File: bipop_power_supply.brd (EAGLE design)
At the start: 82.5 x 70.8 mm, 33 parts, among them IC1 LM1117MP-3.3, IC2 LM1117MP-5.0, X2 MSTBA6

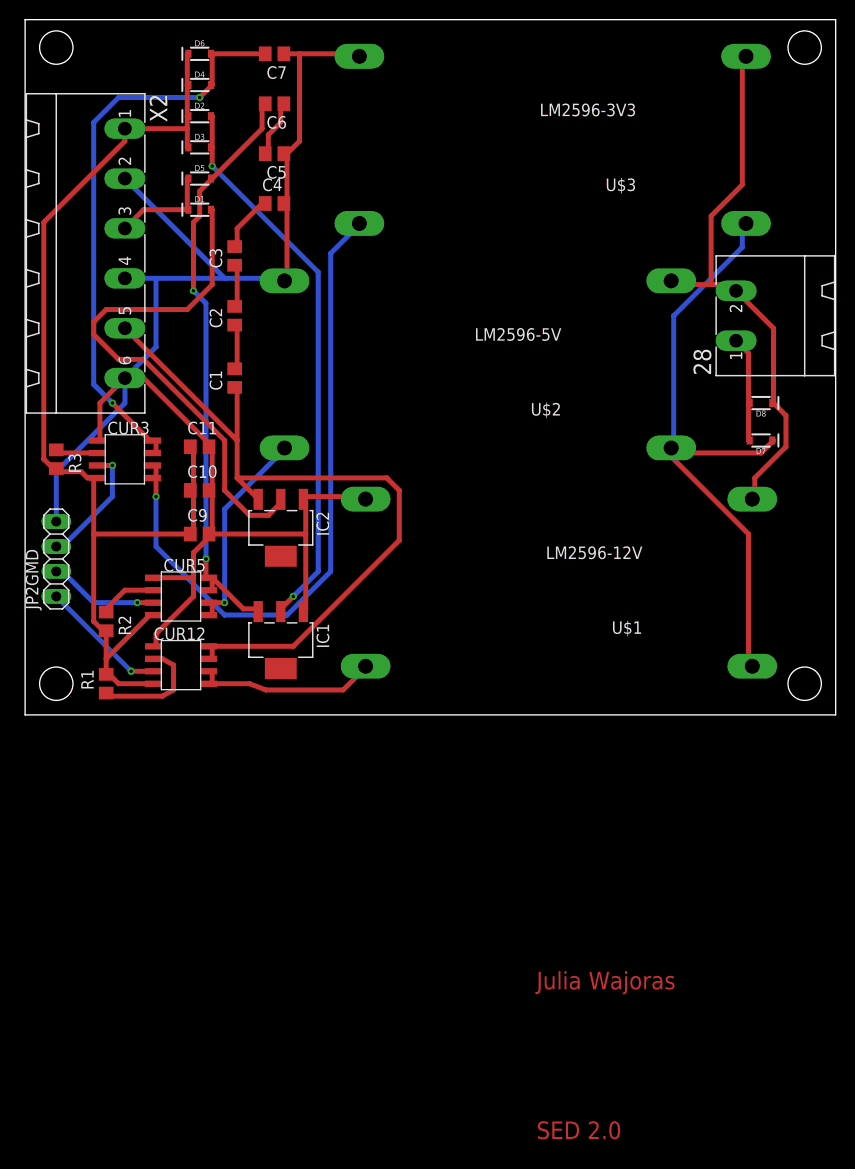
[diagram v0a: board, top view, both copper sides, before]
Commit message: Minor PoSup layout  changes
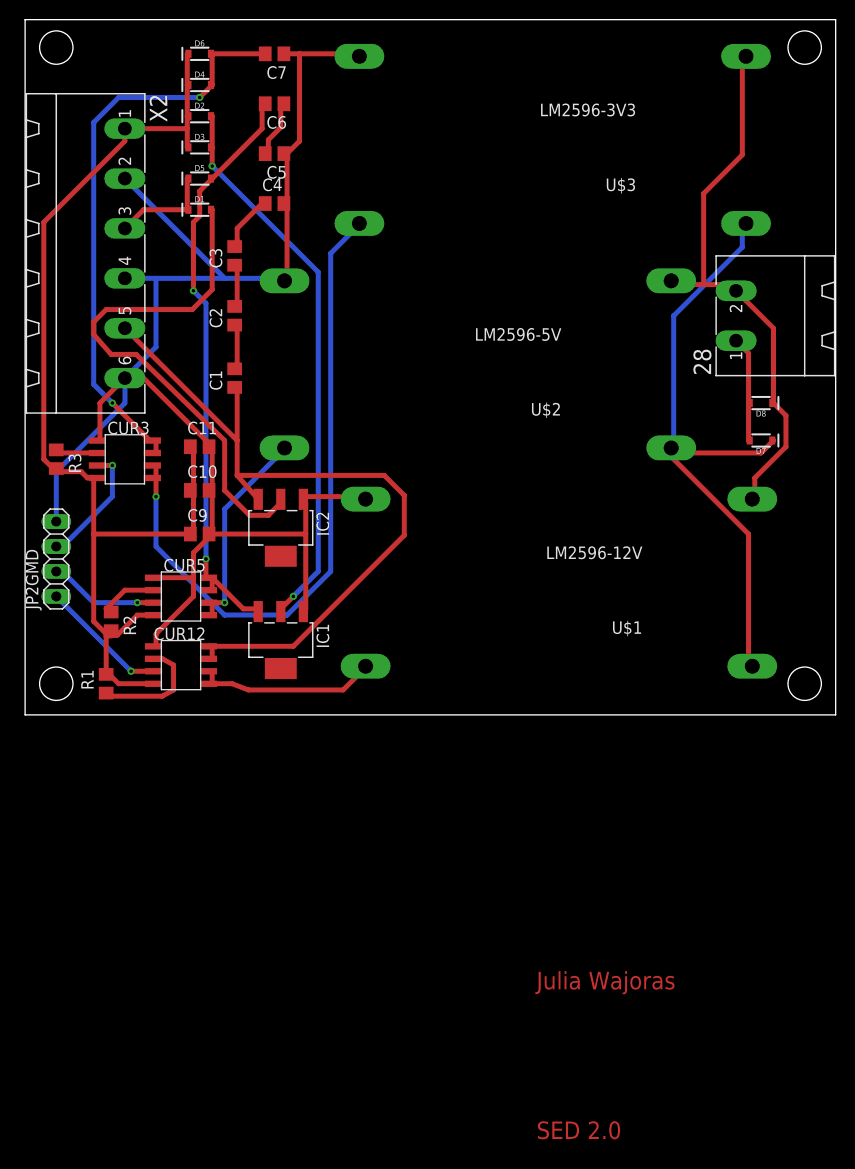
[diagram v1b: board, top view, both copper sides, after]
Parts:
- moved R2 0.51 mm to (12.6, 9.53)
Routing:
- net VCC_3V3: track 112.5 -> 111.8 mm
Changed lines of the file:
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@@
 <?xml version="1.0" encoding="utf-8"?>
 <!DOCTYPE eagle SYSTEM "eagle.dtd">
-<eagle version="8.3.2">
+<eagle version="8.5.1">
 <drawing>
 <settings>
@@
 <param name="dpMaxLengthDifference" value="10mm"/>
 <param name="dpGapFactor" value="2.5"/>
-<param name="checkGrid" value="0"/>
 <param name="checkAngle" value="0"/>
 <param name="checkFont" value="1"/>
 <param name="checkRestrict" value="1"/>
+<param name="checkStop" value="0"/>
+<param name="checkValues" value="0"/>
 <param name="useDiameter" value="13"/>
 <param name="maxErrors" value="50"/>
@@
 <element name="C11" library="rcl" library_urn="urn:adsk.eagle:library:334" package="C0805" package3d_urn="urn:adsk.eagle:package:23617/2" value="0.1uF" x="21.59" y="27.305"/>
 <element name="R1" library="rcl" library_urn="urn:adsk.eagle:library:334" package="R0805" package3d_urn="urn:adsk.eagle:package:23553/2" value="4.7k" x="12.065" y="3.175" rot="R90"/>
-<element name="R2" library="rcl" library_urn="urn:adsk.eagle:library:334" package="R0805" package3d_urn="urn:adsk.eagle:package:23553/2" value="4.7k" x="12.065" y="9.525" rot="R270"/>
+<element name="R2" library="rcl" library_urn="urn:adsk.eagle:library:334" package="R0805" package3d_urn="urn:adsk.eagle:package:23553/2" value="4.7k" x="12.573" y="9.525" rot="R270"/>
 <element name="R3" library="rcl" library_urn="urn:adsk.eagle:library:334" package="R0805" package3d_urn="urn:adsk.eagle:package:23553/2" value="4.7k" x="6.985" y="26.035" rot="R270"/>
 </elements>
@@
 <contactref element="D1" pad="A"/>
 <contactref element="IC2" pad="2"/>
-<wire x1="22.86" y1="43.815" x2="22.86" y2="51.435" width="0.508" layer="1"/>
-<wire x1="20.32" y1="41.275" x2="22.86" y2="43.815" width="0.508" layer="1"/>
-<wire x1="12.065" y1="41.275" x2="20.32" y2="41.275" width="0.508" layer="1"/>
+<wire x1="22.86" y1="43.307" x2="22.86" y2="51.435" width="0.508" layer="1"/>
+<wire x1="20.828" y1="41.275" x2="22.86" y2="43.307" width="0.508" layer="1"/>
+<wire x1="12.065" y1="41.275" x2="20.828" y2="41.275" width="0.508" layer="1"/>
 <wire x1="10.795" y1="40.005" x2="12.065" y2="41.275" width="0.508" layer="1"/>
 <wire x1="10.795" y1="38.735" x2="10.795" y2="40.005" width="0.508" layer="1"/>
-<wire x1="13.335" y1="36.195" x2="10.795" y2="38.735" width="0.508" layer="1"/>
-<wire x1="15.875" y1="36.195" x2="13.335" y2="36.195" width="0.508" layer="1"/>
-<wire x1="24.13" y1="27.94" x2="15.875" y2="36.195" width="0.508" layer="1"/>
+<wire x1="12.573" y1="36.703" x2="10.795" y2="38.735" width="0.508" layer="1"/>
+<wire x1="15.113" y1="36.703" x2="12.573" y2="36.703" width="0.508" layer="1"/>
+<wire x1="24.13" y1="27.94" x2="15.113" y2="36.703" width="0.508" layer="1"/>
 <wire x1="24.13" y1="22.86" x2="24.13" y2="27.94" width="0.508" layer="1"/>
 <wire x1="26.67" y1="20.32" x2="24.13" y2="22.86" width="0.508" layer="1"/>
@@
 <wire x1="10.16" y1="24.13" x2="9.525" y2="24.765" width="0.508" layer="1"/>
 <wire x1="10.795" y1="24.13" x2="10.16" y2="24.13" width="0.508" layer="1"/>
-<wire x1="12.065" y1="8.255" x2="12.065" y2="5.715" width="0.508" layer="1"/>
-<wire x1="12.065" y1="5.715" x2="12.065" y2="4.445" width="0.508" layer="1"/>
+<wire x1="12.065" y1="8.255" x2="12.065" y2="8.001" width="0.508" layer="1"/>
+<wire x1="12.065" y1="8.001" x2="12.065" y2="4.445" width="0.508" layer="1"/>
 <wire x1="13.335" y1="3.175" x2="16.51" y2="3.175" width="0.508" layer="1"/>
 <wire x1="12.065" y1="4.445" x2="13.335" y2="3.175" width="0.508" layer="1"/>
 <wire x1="16.51" y1="3.175" x2="16.885" y2="3.17" width="0.508" layer="1"/>
 <wire x1="12.065" y1="4.445" x2="12.065" y2="4.125" width="0.508" layer="1"/>
-<wire x1="12.065" y1="5.715" x2="16.51" y2="10.16" width="0.508" layer="1"/>
+<wire x1="12.065" y1="8.001" x2="13.208" y2="8.128" width="0.508" layer="1"/>
+<wire x1="13.208" y1="8.128" x2="15.24" y2="10.16" width="0.508" layer="1"/>
+<wire x1="15.24" y1="10.16" x2="16.51" y2="10.16" width="0.508" layer="1"/>
 <wire x1="16.51" y1="10.16" x2="16.885" y2="10.155" width="0.508" layer="1"/>
 <wire x1="10.795" y1="9.525" x2="10.795" y2="18.415" width="0.508" layer="1"/>
@@
 <wire x1="12.065" y1="8.255" x2="10.795" y2="9.525" width="0.508" layer="1"/>
 <wire x1="10.795" y1="24.13" x2="11.17" y2="24.125" width="0.508" layer="1"/>
-<wire x1="12.065" y1="8.255" x2="12.065" y2="8.575" width="0.508" layer="1"/>
+<wire x1="12.065" y1="8.255" x2="12.573" y2="8.575" width="0.508" layer="1"/>
 <wire x1="10.795" y1="18.415" x2="20.64" y2="18.415" width="0.508" layer="1"/>
 <wire x1="13.97" y1="58.42" x2="13.97" y2="59.69" width="0.508" layer="1"/>
@@
 <contactref element="C5" pad="2"/>
 <contactref element="C6" pad="1"/>
-<wire x1="28.575" y1="59.055" x2="28.575" y2="57.15" width="0.508" layer="1"/>
-<wire x1="29.845" y1="60.325" x2="28.575" y2="59.055" width="0.508" layer="1"/>
-<wire x1="29.845" y1="62.23" x2="29.845" y2="60.325" width="0.508" layer="1"/>
+<wire x1="28.575" y1="58.547" x2="28.575" y2="57.15" width="0.508" layer="1"/>
+<wire x1="29.845" y1="59.817" x2="28.575" y2="58.547" width="0.508" layer="1"/>
+<wire x1="29.845" y1="62.23" x2="29.845" y2="59.817" width="0.508" layer="1"/>
 <wire x1="28.575" y1="57.15" x2="28.26" y2="57.15" width="0.508" layer="1"/>
 <wire x1="29.845" y1="62.23" x2="30.16" y2="62.23" width="0.508" layer="1"/>
@@
 <wire x1="78.105" y1="22.225" x2="77.851" y2="21.971" width="0.508" layer="1"/>
 <wire x1="80.01" y1="31.75" x2="79.89" y2="31.75" width="0.508" layer="1"/>
-<wire x1="75.565" y1="43.815" x2="73.66" y2="43.815" width="0.508" layer="1"/>
-<wire x1="73.66" y1="43.815" x2="69.85" y2="43.815" width="0.508" layer="1"/>
+<wire x1="75.565" y1="43.815" x2="72.898" y2="43.815" width="0.508" layer="1"/>
+<wire x1="72.898" y1="43.815" x2="69.85" y2="43.815" width="0.508" layer="1"/>
 <wire x1="76.2" y1="43.18" x2="75.565" y2="43.815" width="0.508" layer="1"/>
 <wire x1="69.85" y1="43.815" x2="69.596" y2="44.196" width="0.508" layer="1"/>
-<wire x1="76.835" y1="53.975" x2="76.835" y2="66.675" width="0.508" layer="1"/>
-<wire x1="73.66" y1="50.8" x2="76.835" y2="53.975" width="0.508" layer="1"/>
-<wire x1="73.66" y1="43.815" x2="73.66" y2="50.8" width="0.508" layer="1"/>
+<wire x1="76.835" y1="57.023" x2="76.835" y2="66.675" width="0.508" layer="1"/>
+<wire x1="72.898" y1="53.086" x2="76.835" y2="57.023" width="0.508" layer="1"/>
+<wire x1="72.898" y1="43.815" x2="72.898" y2="53.086" width="0.508" layer="1"/>
 <wire x1="76.835" y1="66.675" x2="77.216" y2="67.056" width="0.508" layer="1"/>
 </signal>
@@
 <wire x1="22.86" y1="6.985" x2="22.86" y2="5.715" width="0.508" layer="1"/>
 <wire x1="22.86" y1="5.715" x2="22.485" y2="5.71" width="0.508" layer="1"/>
-<wire x1="25.4" y1="24.13" x2="25.4" y2="27.94" width="0.508" layer="1"/>
+<wire x1="25.4" y1="24.384" x2="25.4" y2="27.94" width="0.508" layer="1"/>
 <wire x1="25.4" y1="27.94" x2="25.4" y2="33.02" width="0.508" layer="1"/>
-<wire x1="27.305" y1="22.225" x2="25.4" y2="24.13" width="0.508" layer="1"/>
+<wire x1="27.305" y1="22.225" x2="25.4" y2="24.384" width="0.508" layer="1"/>
 <wire x1="25.4" y1="33.02" x2="25.146" y2="33.34" width="0.508" layer="1"/>
 <wire x1="27.305" y1="22.225" x2="27.545" y2="21.95" width="0.508" layer="1"/>
 <wire x1="31.115" y1="6.985" x2="22.86" y2="6.985" width="0.508" layer="1"/>
-<wire x1="41.91" y1="17.78" x2="31.115" y2="6.985" width="0.508" layer="1"/>
-<wire x1="41.91" y1="22.86" x2="41.91" y2="17.78" width="0.508" layer="1"/>
-<wire x1="40.64" y1="24.13" x2="41.91" y2="22.86" width="0.508" layer="1"/>
-<wire x1="25.4" y1="24.13" x2="40.64" y2="24.13" width="0.508" layer="1"/>
+<wire x1="42.418" y1="18.288" x2="31.115" y2="6.985" width="0.508" layer="1"/>
+<wire x1="42.418" y1="22.352" x2="42.418" y2="18.288" width="0.508" layer="1"/>
+<wire x1="40.386" y1="24.384" x2="42.418" y2="22.352" width="0.508" layer="1"/>
+<wire x1="25.4" y1="24.384" x2="40.386" y2="24.384" width="0.508" layer="1"/>
 <wire x1="22.86" y1="6.985" x2="22.485" y2="6.98" width="0.508" layer="1"/>
 <wire x1="25.4" y1="27.94" x2="13.97" y2="39.37" width="0.508" layer="1"/>
@@
 <wire x1="22.86" y1="4.445" x2="22.86" y2="3.175" width="0.508" layer="1"/>
 <wire x1="22.86" y1="4.445" x2="22.485" y2="4.44" width="0.508" layer="1"/>
-<wire x1="26.67" y1="3.175" x2="22.86" y2="3.175" width="0.508" layer="1"/>
-<wire x1="28.321" y1="2.54" x2="26.67" y2="3.175" width="0.508" layer="1"/>
-<wire x1="36.195" y1="2.54" x2="28.321" y2="2.54" width="0.508" layer="1"/>
+<wire x1="24.892" y1="3.175" x2="22.86" y2="3.175" width="0.508" layer="1"/>
+<wire x1="26.543" y1="2.54" x2="24.892" y2="3.175" width="0.508" layer="1"/>
+<wire x1="36.195" y1="2.54" x2="26.543" y2="2.54" width="0.508" layer="1"/>
 <wire x1="38.1" y1="4.445" x2="36.195" y2="2.54" width="0.508" layer="1"/>
 <wire x1="22.86" y1="3.175" x2="22.485" y2="3.17" width="0.508" layer="1"/>
@@
 <wire x1="13.97" y1="12.7" x2="12.065" y2="10.795" width="0.508" layer="1"/>
 <wire x1="16.51" y1="12.7" x2="13.97" y2="12.7" width="0.508" layer="1"/>
-<wire x1="12.065" y1="10.795" x2="12.065" y2="10.475" width="0.508" layer="1"/>
+<wire x1="12.065" y1="10.795" x2="12.573" y2="10.475" width="0.508" layer="1"/>
 <wire x1="16.51" y1="12.7" x2="16.885" y2="12.695" width="0.508" layer="1"/>
 </signal>
